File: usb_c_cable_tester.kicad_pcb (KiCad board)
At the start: 2 copper layers, 85.6 x 54 mm, 58 parts, among them J1 USB C, J2 USB C, J3 USB_B_Micro, J4 USB3_B, J5 USB_B_Mini, J6 USB3_A

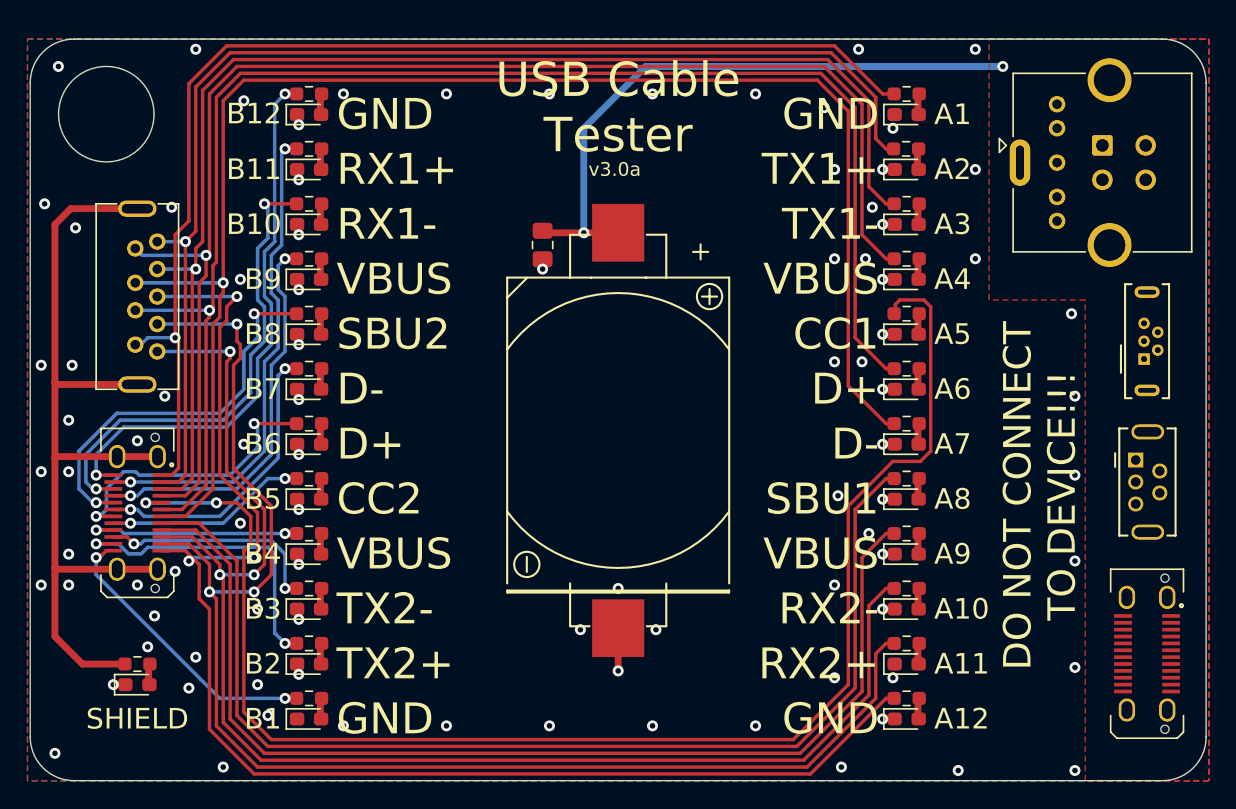
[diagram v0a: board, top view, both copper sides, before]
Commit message: New MicroB part with long pins. Added Battery test. Spacing. Cleaned up routing. v3.0b
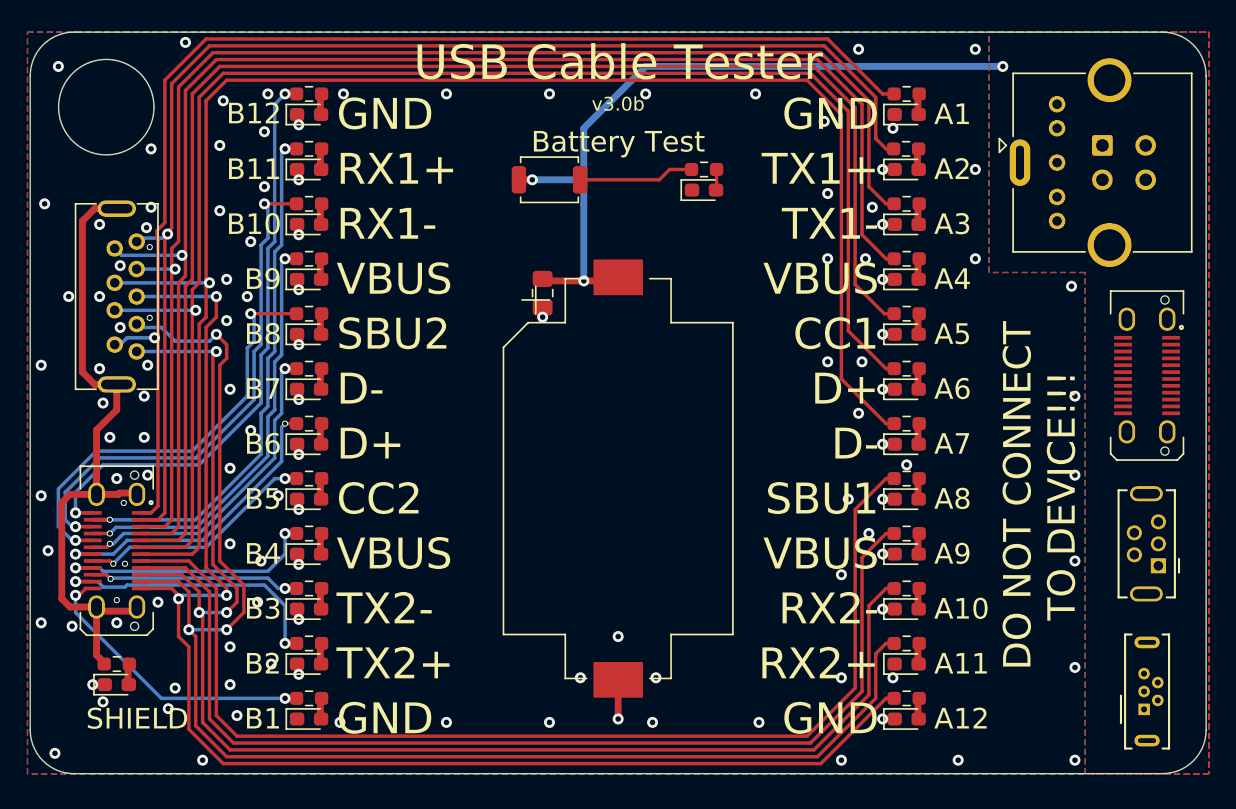
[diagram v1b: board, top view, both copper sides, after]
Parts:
- added D26: LED, LED_SMD:LED_0603_1608Metric_Pad1.05x0.95mm_HandSolder, F.Cu at (106.2, 84.0)
- added R26: 2.2k, Resistor_SMD:R_0603_1608Metric_Pad0.98x0.95mm_HandSolder, F.Cu at (106.2, 82.5)
- added SW1: Battery, Button_Switch_SMD:SW_SPST_TS-1088-xR020, F.Cu at (95.0, 83.2)
- BT1: footprint easyeda:BAT-TH_CR2032-BS-6-1 -> Battery:BatteryHolder_Keystone_1060_1x2032
- moved J3 25.5 mm to (138.3, 121.8)
- moved J1 20.2 mm to (138.5, 97.5)
- moved J5 7.87 mm to (139.3, 111.3), turned to 90 degrees
- moved BT1 3.50 mm to (100.0, 105.0), turned to -90 degrees
- moved C1 3.50 mm to (94.5, 91.5)
- moved J2 3.13 mm to (63.5, 110.2)
- moved D21 1.50 mm to (63.5, 120.0)
- moved J6 1.50 mm to (63.5, 91.8)
- moved R21 1.50 mm to (63.5, 118.5)
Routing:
- net /SHLD: track 63.6 -> 48.5 mm
- net Net-(R26-Pad1): track 0.00 -> 8.42 mm
- net +3V3: track 45.5 -> 53.7 mm, vias 2 -> 3
- net /D-_A: track 111.2 -> 116.7 mm
- net /TX1+: track 89.1 -> 94.7 mm
- net /VBUS_A4: track 98.9 -> 104.4 mm
- net /D+_A: track 106.8 -> 112.2 mm
- net /TX1-: track 93.3 -> 98.6 mm
- net /GND_A1: track 87.1 -> 92.1 mm
- net /VBUS_B4: track 16.0 -> 19.5 mm
- net /SBU2: track 28.7 -> 31.9 mm
- net /CC2: track 14.8 -> 17.6 mm
- net /GND_B12: track 40.4 -> 43.1 mm
- net /RX1-: track 35.3 -> 37.9 mm
- net /CC1: track 104.9 -> 102.6 mm, vias 2 -> 0
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- added copper zone on B.Cu, net +3V3
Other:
- board text added: "Battery Test"
- board text added: "v3.0b"
- board text removed: "v3.0a"
